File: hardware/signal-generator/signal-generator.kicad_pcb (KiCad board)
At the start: 4 copper layers, 135 parts, among them J1 AVR-ISP-6, J10 Output_Conn, J11 SD_Card_Conn, J12 TP_Conn, J13 LCD_Conn, J2 AVR_SPI, J3 PORT_G, J4 PORT_F, J5 PORT_E, J6 PORT_A, J7 PORT_C, J8 AREF, J9 Power_Supply_Rails, Q1 AP2310GN, Q2 AP2310GN, Q3 AP2310GN, Q4 AP2310GN, Q5 AP2310GN, Q6 AP2310GN, Q7 AP2310GN, Q8 AP2310GN, Q9 AP2310GN, SW1 RESET_BUTTON, U1 74HC04, U10 MCP23017-E/SO, U11 AD9764AR, U12 TS4061AICT-1.25, U13 74HC4040, U14 74HC4040, U15 MCP4651-502E/ST, U16 AZ431AN-A, U17 AD8021ARZ, U18 MCP4551-103E/MS, U19 AD8021ARZ, U2 74HC08, U20 AD8021ARZ, U21 AD8021ARZ, U3 74HC08, U4 74HC30, U5 ATmega2561-16AU, U6 ADP7142AUJZ-5.0, U7 TC1017-3.3VCTTR, U8 DS1085Z-10+, U9 CY7C1021D-10ZSXI, Y1 16MHz

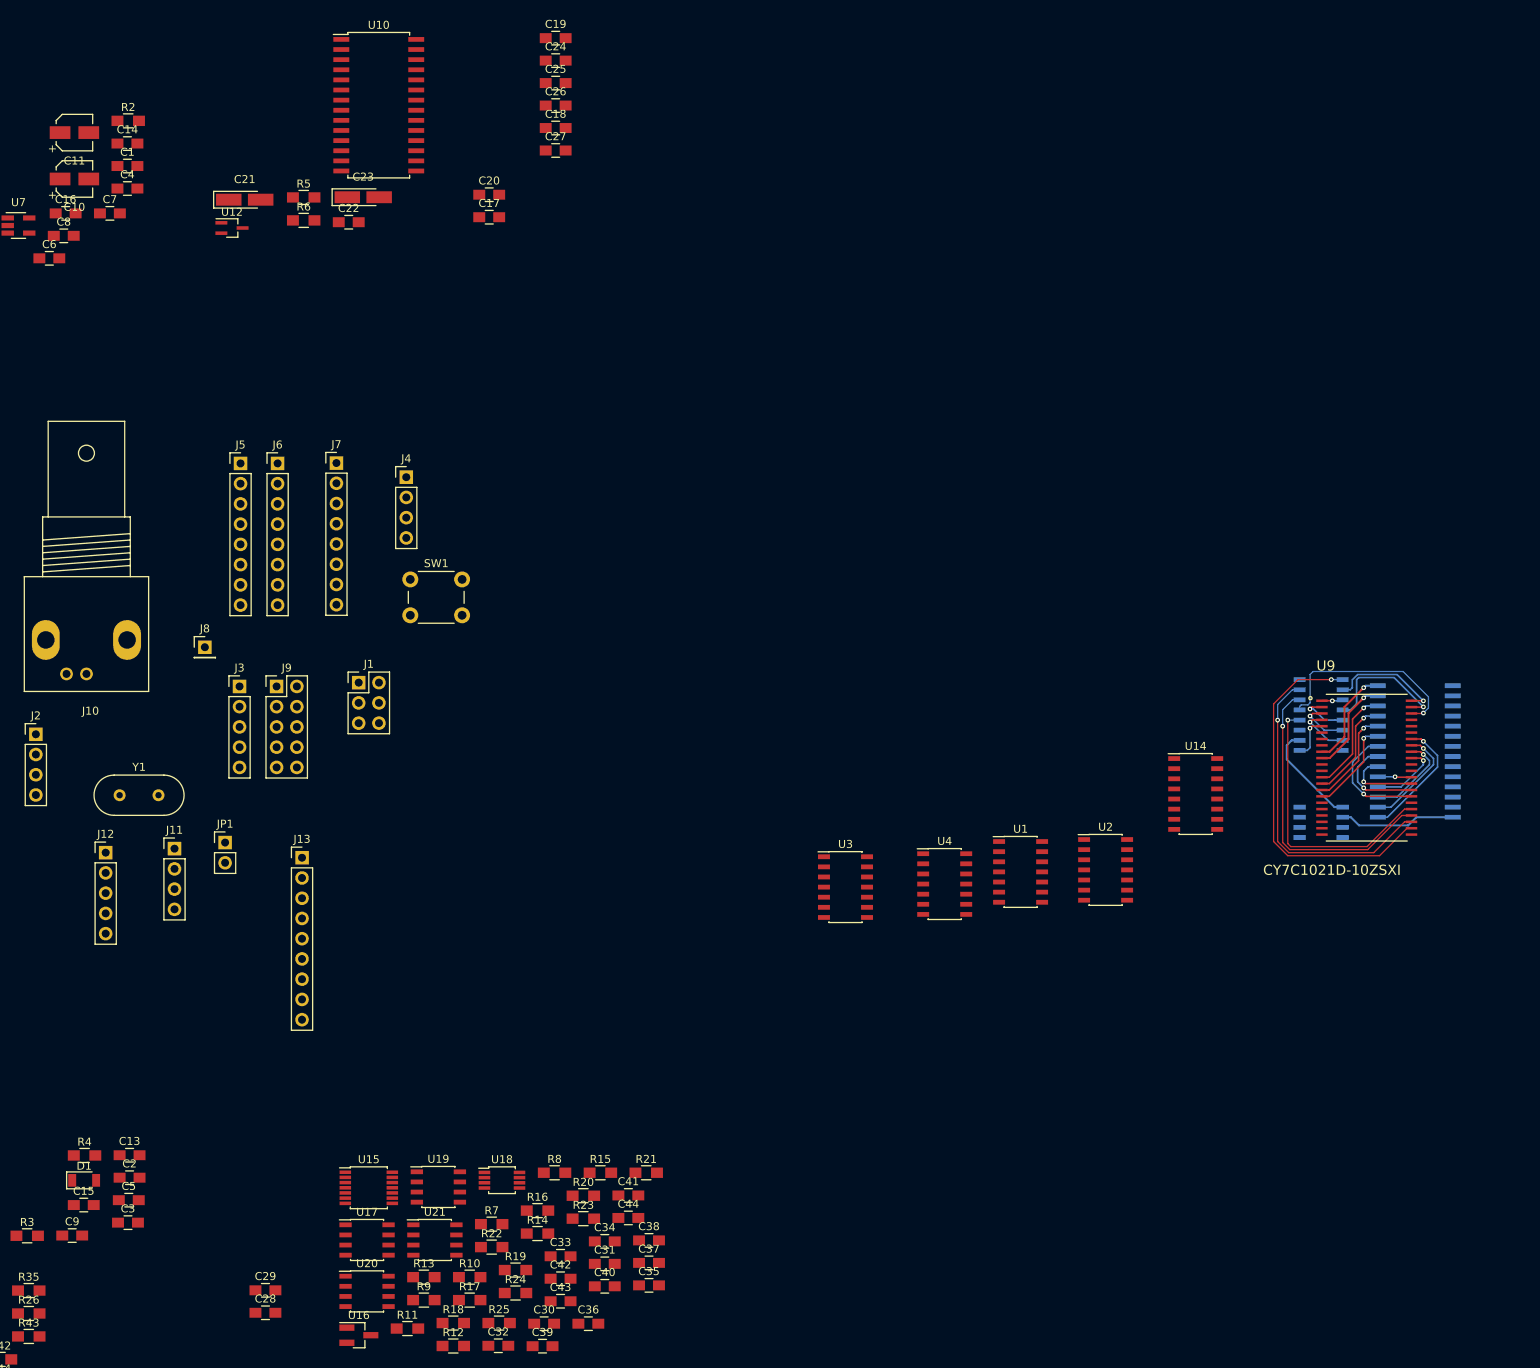
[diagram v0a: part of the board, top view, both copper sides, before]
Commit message: [Signal Generator] Complete DDS system layout and routing
All components of the DDS system, as well as their supporting parts, are
laid out compactly on the board.
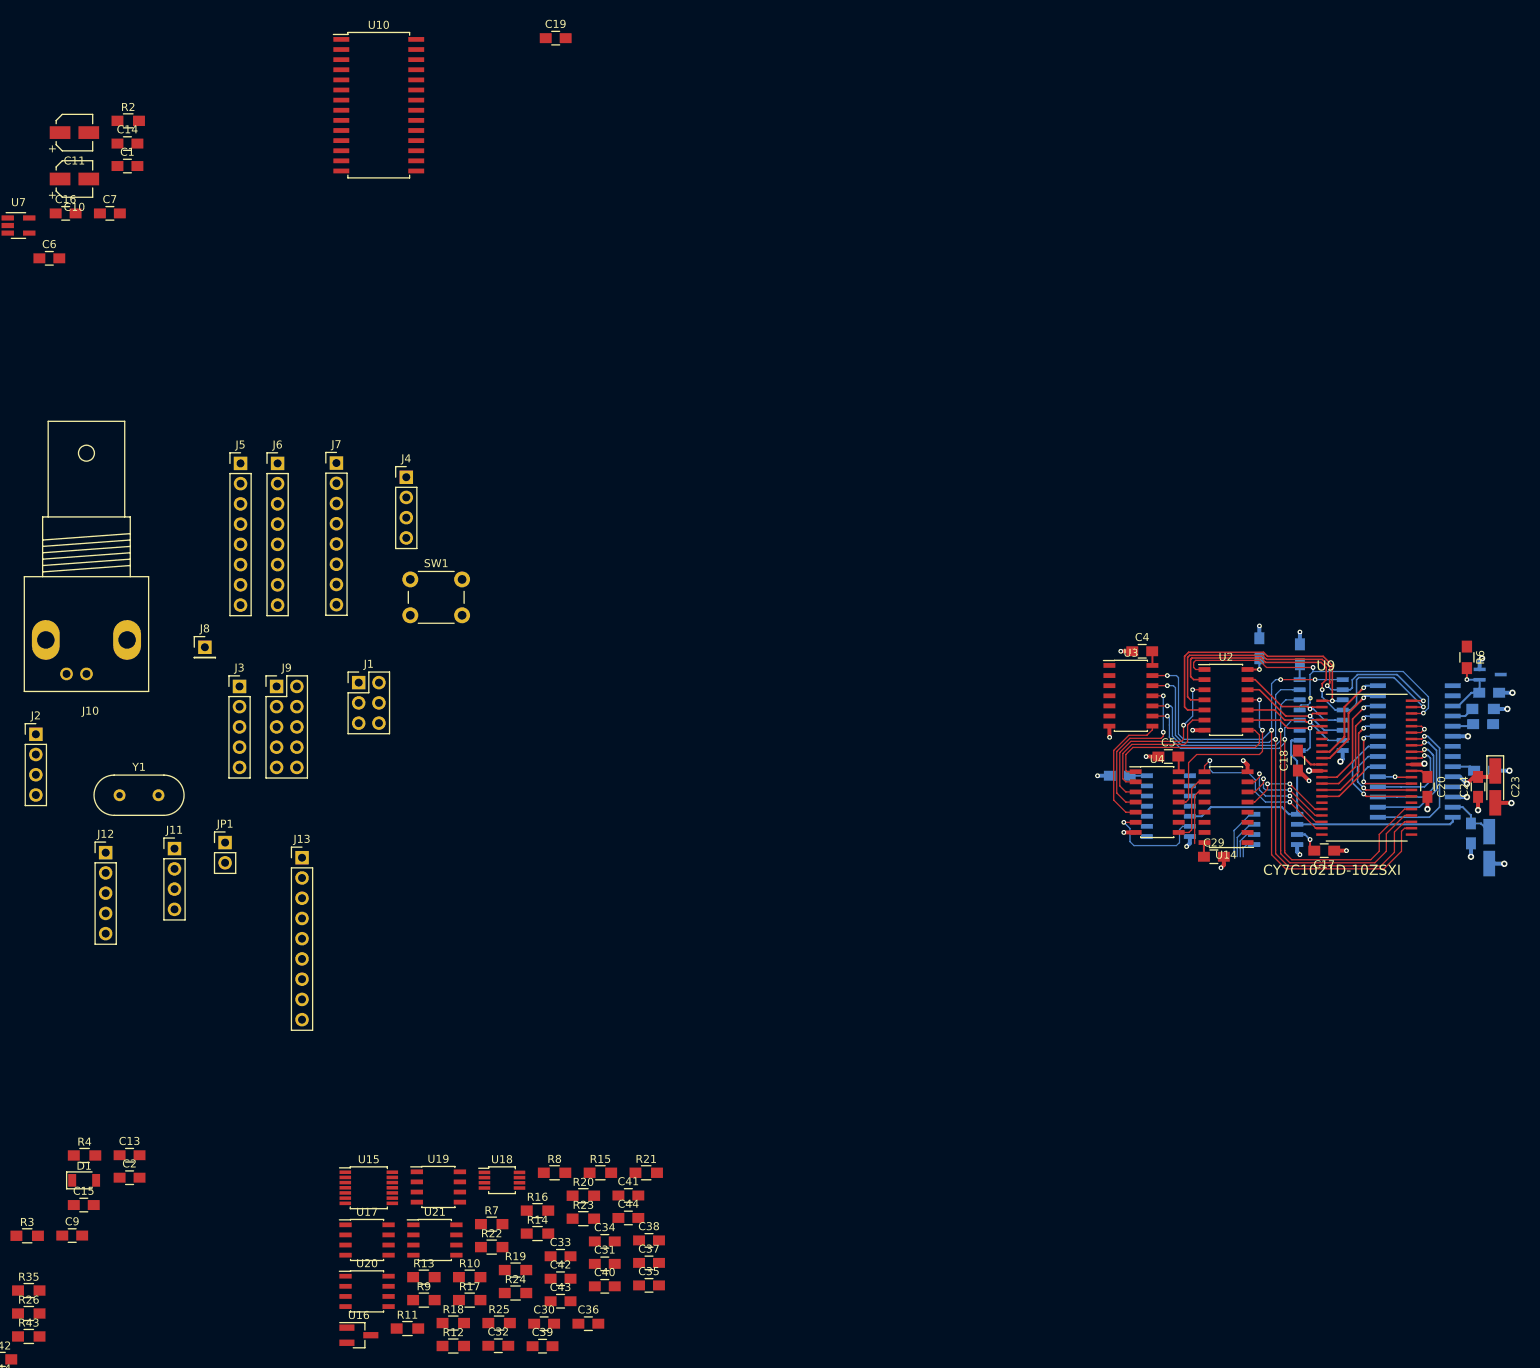
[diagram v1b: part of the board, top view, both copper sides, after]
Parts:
- C21, C22, C25, C26, C27, C28, C3, C8, R5, U1, U12: moved to B.Cu
- moved C21 176.1 mm to (150.7, 80.0), turned to 270 degrees
- moved U12 167.5 mm to (150.9, 58.3)
- moved R5 161.3 mm to (150.0, 62.6)
- moved C22 160.4 mm to (148.5, 78.2), turned to 270 degrees
- moved C23 160.2 mm to (151.5, 72.4), turned to 270 degrees
- moved C3 159.2 mm to (121.9, 55.0), turned to 270 degrees
- moved R6 155.9 mm to (148.0, 56.1), turned to 270 degrees
- moved C28 153.9 mm to (127.0, 55.8), turned to 90 degrees
- moved C8 148.8 mm to (104.4, 71.0)
- moved C24 147.3 mm to (149.4, 72.4), turned to 90 degrees
- moved C25 145.0 mm to (150.1, 70.4), turned to 180 degrees
- moved C5 141.8 mm to (110.5, 68.6)
- moved C4 140.0 mm to (107.2, 55.4)
- moved C26 139.9 mm to (150.0, 64.5), turned to 180 degrees
- moved C20 139.2 mm to (143.0, 72.4), turned to 270 degrees
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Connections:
- U1 pad 1: /~CP -> Net-(U1-Pad1)
- U1 pad 12: Net-(U1-Pad12) -> /Output Circuitry/~DISABLE
- U1 pad 13: Net-(U1-Pad13) -> /PWRDWN
- U1 pad 2: /DDS System/16-bit Counter/CP2I6 -> Net-(U1-Pad2)
- U1 pad 5: /PWRDWN -> /~CP
- U1 pad 6: /Output Circuitry/~DISABLE -> /DDS System/16-bit Counter/CP2I6
- U2 pad 1: /DDS System/16-bit Counter/Q1 -> /DDS System/16-bit Counter/Q7
- U2 pad 10: Net-(U2-Pad10) -> /DDS System/16-bit Counter/Q1
- U2 pad 11: Net-(U2-Pad11) -> /DDS System/16-bit Counter/CP2I0
- U2 pad 12: Net-(U2-Pad12) -> /DDS System/16-bit Counter/Q2
- U2 pad 13: Net-(U2-Pad13) -> /DDS System/16-bit Counter/Q3
- U2 pad 2: /DDS System/16-bit Counter/Q0 -> /DDS System/16-bit Counter/Q6
- U2 pad 3: /DDS System/16-bit Counter/CP2I5 -> /DDS System/16-bit Counter/CP2I3
- U2 pad 4: /DDS System/16-bit Counter/Q3 -> /DDS System/16-bit Counter/Q5
- U2 pad 5: /DDS System/16-bit Counter/Q2 -> /DDS System/16-bit Counter/Q4
- U2 pad 6: /DDS System/16-bit Counter/CP2I4 -> /DDS System/16-bit Counter/CP2I2
- U2 pad 8: Net-(U2-Pad8) -> /DDS System/16-bit Counter/CP2I1
- U2 pad 9: Net-(U2-Pad9) -> /DDS System/16-bit Counter/Q0
- U3 pad 1: /DDS System/16-bit Counter/Q9 -> Net-(U3-Pad1)
- U3 pad 10: /DDS System/16-bit Counter/Q4 -> /DDS System/16-bit Counter/Q9
- U3 pad 11: /DDS System/16-bit Counter/CP2I2 -> /DDS System/16-bit Counter/CP2I4
- U3 pad 12: /DDS System/16-bit Counter/Q7 -> /DDS System/16-bit Counter/Q10
- U3 pad 13: /DDS System/16-bit Counter/Q6 -> /DDS System/16-bit Counter/Q11
- U3 pad 2: /DDS System/16-bit Counter/Q8 -> Net-(U3-Pad2)
- U3 pad 3: /DDS System/16-bit Counter/CP2I1 -> Net-(U3-Pad3)
- U3 pad 4: /DDS System/16-bit Counter/Q11 -> Net-(U3-Pad4)
- U3 pad 5: /DDS System/16-bit Counter/Q10 -> Net-(U3-Pad5)
- U3 pad 6: /DDS System/16-bit Counter/CP2I0 -> Net-(U3-Pad6)
- U3 pad 8: /DDS System/16-bit Counter/CP2I3 -> /DDS System/16-bit Counter/CP2I5
- U3 pad 9: /DDS System/16-bit Counter/Q5 -> /DDS System/16-bit Counter/Q8
- U4 pad 1: /DDS System/16-bit Counter/CP2I0 -> /DDS System/16-bit Counter/CP2I1
- U4 pad 11: /DDS System/16-bit Counter/CP2I6 -> /DDS System/16-bit Counter/CP2I0
- U4 pad 2: /DDS System/16-bit Counter/CP2I1 -> /DDS System/16-bit Counter/CP2I2
- U4 pad 3: /DDS System/16-bit Counter/CP2I2 -> /DDS System/16-bit Counter/CP2I3
- U4 pad 4: /DDS System/16-bit Counter/CP2I3 -> /DDS System/16-bit Counter/CP2I4
- U4 pad 5: /DDS System/16-bit Counter/CP2I4 -> /DDS System/16-bit Counter/CP2I5
- U4 pad 6: /DDS System/16-bit Counter/CP2I5 -> /DDS System/16-bit Counter/CP2I6
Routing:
- net AGND: track 0.00 -> 49.3 mm, vias 0 -> 29
- net /DDS System/16-bit Counter/Q4: track 2.67 -> 35.6 mm
- net /DDS System/16-bit Counter/Q5: track 14.4 -> 44.8 mm, vias 1 -> 2
- net /DDS System/16-bit Counter/Q11: track 46.7 -> 75.5 mm, vias 1 -> 4
- net /DDS System/16-bit Counter/Q6: track 16.6 -> 45.4 mm, vias 1 -> 2
- net +5VD: track 0.00 -> 28.6 mm, vias 0 -> 2
- net /DDS System/16-bit Counter/Q10: track 39.7 -> 66.7 mm, vias 1 -> 2
- net /DDS System/16-bit Counter/Q9: track 37.6 -> 63.7 mm, vias 1 -> 2
- net /DDS System/16-bit Counter/CP2I0: track 0.00 -> 24.0 mm, vias 0 -> 2
- net /DDS System/16-bit Counter/Q8: track 34.6 -> 58.5 mm, vias 1 -> 2
- net /DDS System/16-bit Counter/CP2I1: track 0.00 -> 23.5 mm
- net /DDS System/16-bit Counter/CP2I3: track 0.00 -> 23.4 mm, vias 0 -> 2
- net /DDS System/16-bit Counter/Q12: track 0.00 -> 21.8 mm, vias 0 -> 2
- net /DDS System/16-bit Counter/CP2I4: track 0.00 -> 21.1 mm, vias 0 -> 2
- net /DDS System/16-bit Counter/CP2I2: track 0.00 -> 18.1 mm
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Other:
- net class Analog Signal added: clearance 0.15, trace_width 0.25, via_dia 0.6, via_drill 0.3
- net class Analog Supply added: clearance 0.15, trace_width 0.5, via_dia 0.8, via_drill 0.4
- net class Digital Supply added: clearance 0.15, trace_width 0.25, via_dia 0.6, via_drill 0.3
